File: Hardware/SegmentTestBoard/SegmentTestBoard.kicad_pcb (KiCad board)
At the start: 2 copper layers, 34 x 17 mm, 14 parts, among them J101 OUT, J102 IN, U101 SN74HC595, U102 STATE

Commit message: Add revision to silkscreen
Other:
- board text added: "${FULL_REVISION}"
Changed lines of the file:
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@@
       (pts (xy 168.21 123.22) (xy 168.21 110.22))
       (height 2.8)
-      (gr_text "0.5118 in" (at 169.86 116.72 90) (layer "Dwgs.User")
+      (gr_text "13.0000 mm" (at 169.86 116.72 90) (layer "Dwgs.User")
         (effects (font (size 1 1) (thickness 0.15)))
       )
@@
       (pts (xy 158.21 123.22) (xy 168.21 123.22))
       (height 2.9)
-      (gr_text "0.3937 in" (at 163.21 124.97) (layer "Dwgs.User")
+      (gr_text "10.0000 mm" (at 163.21 124.97) (layer "Dwgs.User")
         (effects (font (size 1 1) (thickness 0.15)))
       )
@@
     (effects (font (size 0.5 0.5) (thickness 0.125) bold) (justify right))
   )
+  (gr_text "${FULL_REVISION}" (at 140 125.5) (layer "F.SilkS")
+    (effects (font (size 0.9 0.9) (thickness 0.15) bold) (justify left bottom))
+  )
   (gr_text "DOUT" (at 171.1 118.384) (layer "F.SilkS")

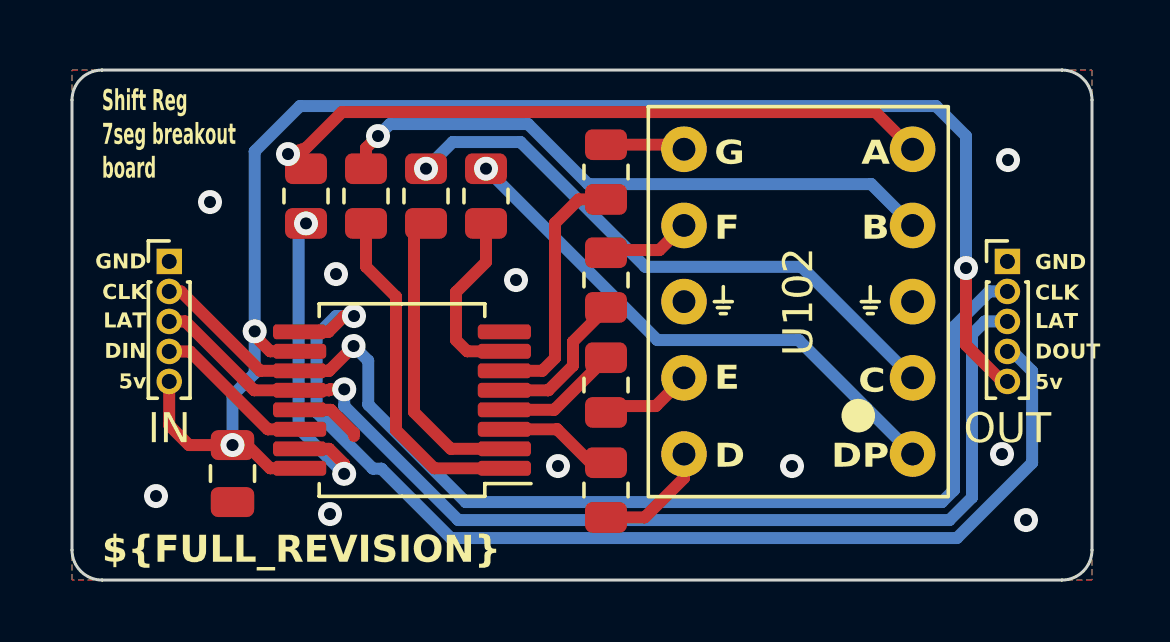
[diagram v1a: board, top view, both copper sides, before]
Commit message: use correct pinheaders
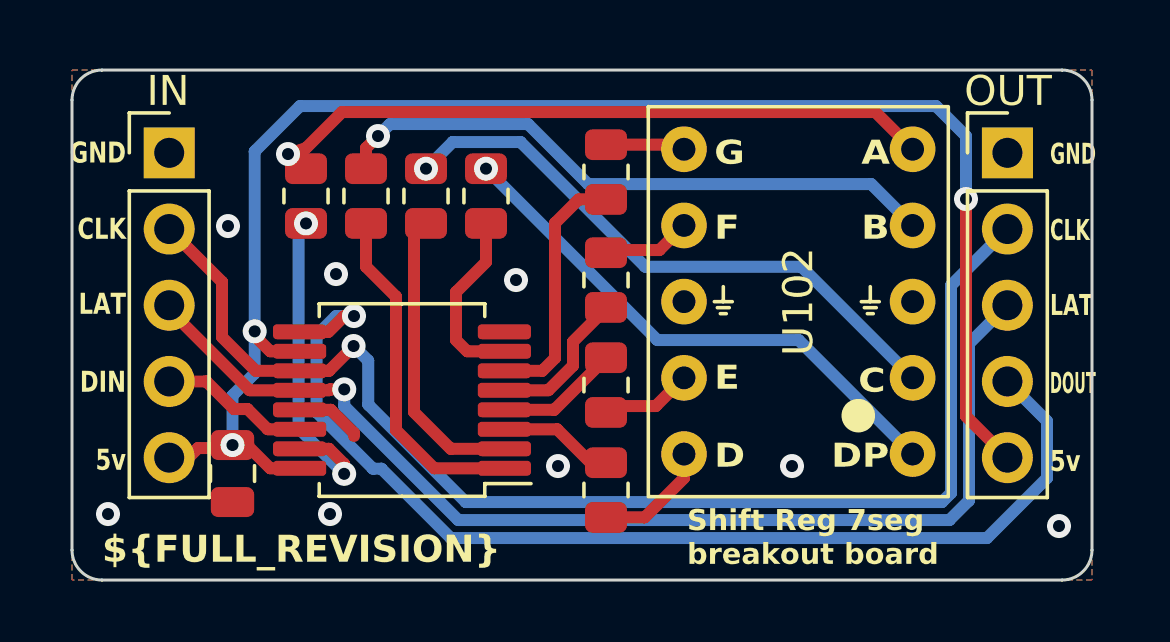
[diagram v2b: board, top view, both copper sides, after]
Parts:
- J101, J102: footprint Connector_PinHeader_1.00mm:PinHeader_1x05_P1.00mm_Vertical -> Connector_PinHeader_2.54mm:PinHeader_1x05_P2.54mm_Vertical
- moved J101 3.62 mm to (170.2, 111.8)
- moved J102 3.62 mm to (142.2, 111.8)
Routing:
- net /CLOCK: track 38.5 -> 42.2 mm
- net +5V: track 52.0 -> 52.8 mm
- net /LATCH: track 37.0 -> 37.8 mm
- net GND: vias 10 -> 9
